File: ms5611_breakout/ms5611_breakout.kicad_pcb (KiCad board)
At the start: 2 copper layers, 12.7 x 10.2 mm, 6 parts, among them P1 CONN_4, P2 CONN_4, U1 MS5611

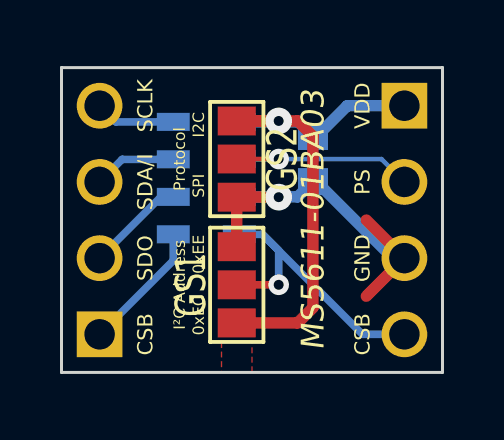
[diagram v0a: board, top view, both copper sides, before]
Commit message: Correcting Gerbers for OSH Park
This version got sent to OSH Park. The silk screen had to be changed
to a min thickness of 5 mills.
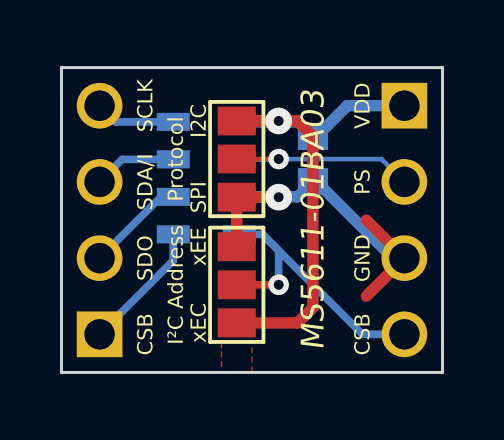
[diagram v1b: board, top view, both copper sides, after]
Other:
- board text added: "1"
- board text added: "xEC"
- board text added: "xEE"
- board text removed: "0xEC"
- board text removed: "0xEE"
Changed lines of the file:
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@@
     (links 17)
     (no_connects 1)
-    (area 344.6272 231.7608 361.4928 242.646201)
+    (area 344.6272 230.4888 361.4928 246.292866)
     (thickness 1.6)
-    (drawings 19)
+    (drawings 20)
     (tracks 53)
     (zones 0)
@@
     (pad_to_mask_clearance 0)
     (aux_axis_origin 0 0)
-    (visible_elements 7FFE7F0F)
+    (visible_elements 7FFFFFFF)
     (pcbplotparams
-      (layerselection 3178497)
+      (layerselection 284196865)
       (usegerberextensions true)
       (excludeedgelayer true)
@@
       (outputformat 1)
       (mirror false)
-      (drillshape 1)
+      (drillshape 0)
       (scaleselection 1)
-      (outputdirectory ""))
+      (outputdirectory gerber/))
   )
   (net 0 "")
@@
     (descr "Double rangee de contacts 2 x 5 pins")
     (tags CONN)
-    (fp_text reference P2 (at 0 2.54 90) (layer B.SilkS)
+    (fp_text reference P2 (at 4.572 -2.54 90) (layer B.SilkS) hide
       (effects (font (size 1.016 1.016) (thickness 0.2032)) (justify mirror))
     )
@@
     (descr "Double rangee de contacts 2 x 5 pins")
     (tags CONN)
-    (fp_text reference P1 (at 0 2.54 270) (layer B.SilkS)
+    (fp_text reference P1 (at -4.064 -2.54 270) (layer B.SilkS) hide
       (effects (font (size 1.016 1.016) (thickness 0.2032)) (justify mirror))
     )
@@
     (descr "Pontet Goute de soudure")
     (attr virtual)
-    (fp_text reference GS2 (at 1.524 0 90) (layer F.SilkS)
+    (fp_text reference GS2 (at 3.81 9.398 90) (layer F.SilkS) hide
       (effects (font (size 1.016 0.762) (thickness 0.127)))
     )
-    (fp_text value GS3 (at 1.524 0 90) (layer F.SilkS) hide
+    (fp_text value GS3 (at 5.588 9.271 90) (layer F.SilkS) hide
       (effects (font (size 0.762 0.762) (thickness 0.127)))
     )
@@
     (descr "Pontet Goute de soudure")
     (attr virtual)
-    (fp_text reference GS1 (at 1.524 0 270) (layer F.SilkS)
-      (effects (font (size 1.016 0.762) (thickness 0.127)))
-    )
-    (fp_text value GS3 (at 1.524 0 270) (layer F.SilkS) hide
+    (fp_text reference GS1 (at 1.524 -4.953 270) (layer F.SilkS) hide
+      (effects (font (size 1 1) (thickness 0.15)))
+    )
+    (fp_text value GS3 (at 0 -4.953 270) (layer F.SilkS) hide
       (effects (font (size 0.762 0.762) (thickness 0.127)))
     )
@@
     (at 355.092 235.204 90)
     (descr "SMT capacitor, 0603")
-    (fp_text reference C1 (at 0 0.635 90) (layer B.SilkS)
-      (effects (font (size 0.20066 0.20066) (thickness 0.04064)) (justify mirror))
-    )
-    (fp_text value 100nF (at 0 -0.635 90) (layer B.SilkS) hide
-      (effects (font (size 0.20066 0.20066) (thickness 0.04064)) (justify mirror))
+    (fp_text reference C1 (at 1.016 1.143 90) (layer B.SilkS) hide
+      (effects (font (size 0.381 0.381) (thickness 0.0508)) (justify mirror))
+    )
+    (fp_text value 100nF (at -0.127 1.016 90) (layer B.SilkS)
+      (effects (font (size 0.508 0.508) (thickness 0.127)) (justify mirror))
     )
     (fp_line (start 0.5588 -0.4064) (end 0.5588 0.4064) (layer B.SilkS) (width 0.127))
@@
   (module ms5611 (layer B.Cu)
     (at 351.536 235.839 180)
-    (fp_text reference U1 (at 0 3.3 180) (layer B.SilkS)
+    (fp_text reference U1 (at -0.127 4.572 180) (layer B.SilkS) hide
       (effects (font (size 1 1) (thickness 0.15)) (justify mirror))
     )
-    (fp_text value MS5611 (at 0 -3.5 180) (layer B.SilkS)
+    (fp_text value MS5611 (at -1.143 -3.81 180) (layer B.SilkS)
       (effects (font (size 1 1) (thickness 0.15)) (justify mirror))
     )
@@
     )
   )
-  (gr_text "I²C Address" (at 350.647 239.395 90) (layer F.SilkS)
-    (effects (font (size 0.381 0.381) (thickness 0.0508)))
-  )
-  (gr_text Protocol (at 350.647 235.204 90) (layer F.SilkS)
-    (effects (font (size 0.381 0.381) (thickness 0.0508)))
+  (gr_text 1 (at 353.441 233.172) (layer B.SilkS)
+    (effects (font (size 0.508 0.508) (thickness 0.1143)) (justify mirror))
+  )
+  (gr_text "I²C Address" (at 350.52 239.395 90) (layer F.SilkS)
+    (effects (font (size 0.508 0.508) (thickness 0.127)))
+  )
+  (gr_text Protocol (at 350.52 235.204 90) (layer F.SilkS)
+    (effects (font (size 0.508 0.508) (thickness 0.127)))
   )
   (gr_text MS5611-01BA03 (at 355.092 237.236 90) (layer F.SilkS)
-    (effects (font (size 0.762 0.762) (thickness 0.1143) italic))
-  )
-  (gr_text SPI (at 351.282 236.093 90) (layer F.SilkS)
-    (effects (font (size 0.381 0.381) (thickness 0.0508)))
-  )
-  (gr_text 0xEE (at 351.282 238.379 90) (layer F.SilkS)
-    (effects (font (size 0.381 0.381) (thickness 0.0508)))
-  )
-  (gr_text 0xEC (at 351.282 240.411 90) (layer F.SilkS)
-    (effects (font (size 0.381 0.381) (thickness 0.0508)))
-  )
-  (gr_text I2C (at 351.282 234.061 90) (layer F.SilkS)
-    (effects (font (size 0.381 0.381) (thickness 0.0508)))
+    (effects (font (size 0.762 0.762) (thickness 0.127) italic))
+  )
+  (gr_text SPI (at 351.282 236.474 90) (layer F.SilkS)
+    (effects (font (size 0.508 0.508) (thickness 0.127)))
+  )
+  (gr_text xEE (at 351.282 238.125 90) (layer F.SilkS)
+    (effects (font (size 0.508 0.508) (thickness 0.127)))
+  )
+  (gr_text xEC (at 351.282 240.665 90) (layer F.SilkS)
+    (effects (font (size 0.508 0.508) (thickness 0.127)))
+  )
+  (gr_text I2C (at 351.282 233.934 90) (layer F.SilkS)
+    (effects (font (size 0.508 0.508) (thickness 0.127)))
   )
   (gr_text SCLK (at 349.504 233.426 90) (layer F.SilkS)
-    (effects (font (size 0.508 0.508) (thickness 0.1143)))
+    (effects (font (size 0.508 0.508) (thickness 0.127)))
   )
   (gr_text SDA/I (at 349.504 235.966 90) (layer F.SilkS)
-    (effects (font (size 0.508 0.508) (thickness 0.1143)))
+    (effects (font (size 0.508 0.508) (thickness 0.127)))
   )
   (gr_text SDO (at 349.504 238.506 90) (layer F.SilkS)
-    (effects (font (size 0.508 0.508) (thickness 0.1143)))
+    (effects (font (size 0.508 0.508) (thickness 0.127)))
   )
   (gr_text CSB (at 349.504 241.046 90) (layer F.SilkS)
-    (effects (font (size 0.508 0.508) (thickness 0.1143)))
+    (effects (font (size 0.508 0.508) (thickness 0.127)))
   )
   (gr_text CSB (at 356.743 241.046 90) (layer F.SilkS)
-    (effects (font (size 0.508 0.508) (thickness 0.1143)))
+    (effects (font (size 0.508 0.508) (thickness 0.127)))
   )
   (gr_text GND (at 356.743 238.506 90) (layer F.SilkS)
-    (effects (font (size 0.508 0.508) (thickness 0.1143)))
+    (effects (font (size 0.508 0.508) (thickness 0.127)))
   )
   (gr_text PS (at 356.743 235.966 90) (layer F.SilkS)
-    (effects (font (size 0.508 0.508) (thickness 0.1143)))
+    (effects (font (size 0.508 0.508) (thickness 0.127)))
   )
   (gr_text VDD (at 356.743 233.426 90) (layer F.SilkS)
-    (effects (font (size 0.508 0.508) (thickness 0.1143)))
+    (effects (font (size 0.508 0.508) (thickness 0.127)))
   )
   (gr_line (start 346.71 232.156) (end 346.71 242.316) (angle 90) (layer Edge.Cuts) (width 0.1))

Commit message: Fixing the 7-bit I2C Address on silk screen
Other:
- board text added: "x76"
- board text added: "x77"
- board text removed: "xEC"
- board text removed: "xEE"
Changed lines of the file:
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@@
-(kicad_pcb (version 3) (host pcbnew "(2013-dec-23)-stable")
+(kicad_pcb (version 3) (host pcbnew "(2013-jul-07)-stable")
   (general
     (links 17)
@@
     (effects (font (size 0.508 0.508) (thickness 0.127)))
   )
-  (gr_text xEE (at 351.282 238.125 90) (layer F.SilkS)
-    (effects (font (size 0.508 0.508) (thickness 0.127)))
-  )
-  (gr_text xEC (at 351.282 240.665 90) (layer F.SilkS)
-    (effects (font (size 0.508 0.508) (thickness 0.127)))
-  )
+  (gr_text x77 (at 351.282 238.125 90) (layer F.SilkS)
+    (effects (font (size 0.508 0.508) (thickness 0.127)))
+  )
+  (gr_text x76 (at 351.282 240.665 90) (layer F.SilkS)
+    (effects (font (size 0.508 0.508) (thickness 0.127)))
+  )
